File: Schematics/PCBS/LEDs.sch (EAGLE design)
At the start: 13 parts, among them IC1 ATMEGA328P-AU, Q1 TRANSISTOR-FET_DMN2004K, Q2 TRANSISTOR-FET_DMN2004K, Q3 TRANSISTOR-FET_DMN2004K, Q4 TRANSISTOR-FET_DMN2004K, Q5 TRANSISTOR-FET_DMN2004K, Q6 TRANSISTOR-FET_DMN2004K, Q7 TRANSISTOR-FET_DMN2004K, Q8 TRANSISTOR-FET_DMN2004K, Q9 TRANSISTOR-FET_DMN2004K

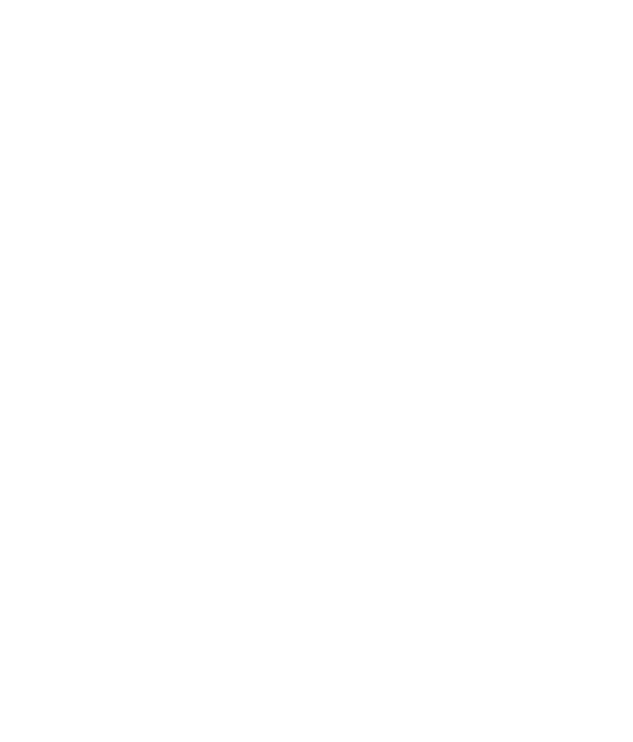
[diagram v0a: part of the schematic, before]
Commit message: added power rail and regulator
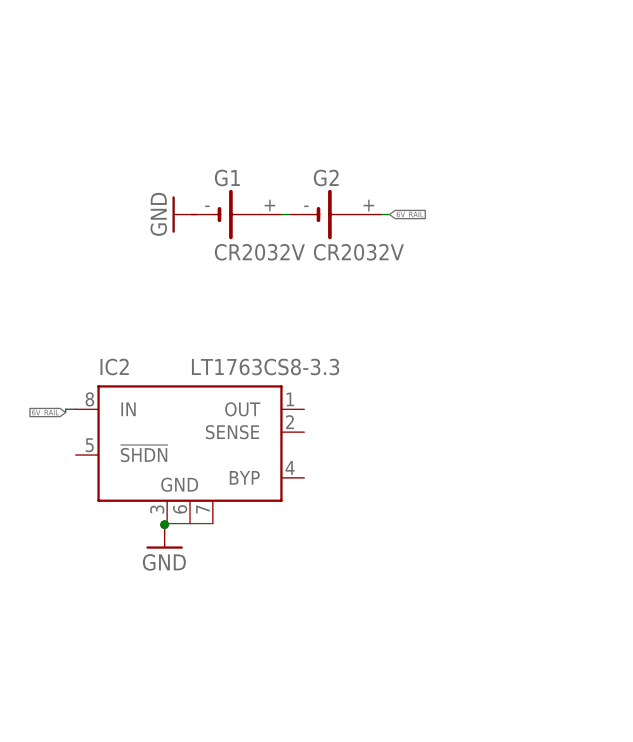
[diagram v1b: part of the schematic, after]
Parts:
- added G1, G2: CR2032V, battery:CR2032V
- added IC2: LT1763CS8-3.3, linear-technology:LT1763CS8-3.3
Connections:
- new net 6V_RAIL: G2.+, IC2.IN
- new net N$19: G1.+, G2.-
- net GND: now also IC2.GND@3
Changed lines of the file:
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@@
 <setting verticaltext="up"/>
 </settings>
-<grid distance="0.1" unitdist="inch" unit="inch" style="lines" multiple="1" display="no" altdistance="0.01" altunitdist="inch" altunit="inch"/>
+<grid distance="1" unitdist="mm" unit="mm" style="lines" multiple="1" display="yes" altdistance="0.000003125" altunitdist="mm" altunit="mm"/>
 <layers>
 <layer number="1" name="Top" color="4" fill="1" visible="no" active="no"/>
@@
 <part name="GND11" library="supply1" library_urn="urn:adsk.eagle:library:371" deviceset="GND" device=""/>
 <part name="GND12" library="supply1" library_urn="urn:adsk.eagle:library:371" deviceset="GND" device=""/>
+<part name="IC2" library="linear-technology" library_urn="urn:adsk.eagle:library:261" deviceset="LT1763CS8" device="" package3d_urn="urn:adsk.eagle:package:16057/2" technology="-3.3"/>
+<part name="GND14" library="supply1" library_urn="urn:adsk.eagle:library:371" deviceset="GND" device=""/>
+<part name="GND13" library="supply1" library_urn="urn:adsk.eagle:library:371" deviceset="GND" device=""/>
+<part name="G1" library="battery" library_urn="urn:adsk.eagle:library:109" deviceset="CR2032V" device="" package3d_urn="urn:adsk.eagle:package:4578/1"/>
+<part name="G2" library="battery" library_urn="urn:adsk.eagle:library:109" deviceset="CR2032V" device="" package3d_urn="urn:adsk.eagle:package:4578/1"/>
 </parts>
 <sheets>
@@
 <attribute name="VALUE" x="596.9" y="-33.02" size="1.778" layer="96" rot="R90"/>
 </instance>
+<instance part="IC2" gate="G$1" x="464.82" y="-43.18" smashed="yes">
+<attribute name="NAME" x="454.66" y="-36.83" size="1.778" layer="95"/>
+<attribute name="VALUE" x="464.82" y="-36.83" size="1.778" layer="96"/>
+</instance>
+<instance part="GND14" gate="1" x="462" y="-56" smashed="yes">
+<attribute name="VALUE" x="459.46" y="-58.54" size="1.778" layer="96"/>
+</instance>
+<instance part="GND13" gate="1" x="463" y="-19" smashed="yes" rot="R270">
+<attribute name="VALUE" x="460.46" y="-16.46" size="1.778" layer="96" rot="R270"/>
+</instance>
+<instance part="G1" gate="1" x="470" y="-19" smashed="yes">
+<attribute name="NAME" x="467.46" y="-15.825" size="1.778" layer="95"/>
+<attribute name="VALUE" x="467.46" y="-24.08" size="1.778" layer="96"/>
+</instance>
+<instance part="G2" gate="1" x="481" y="-19" smashed="yes">
+<attribute name="NAME" x="478.46" y="-15.825" size="1.778" layer="95"/>
+<attribute name="VALUE" x="478.46" y="-24.08" size="1.778" layer="96"/>
+</instance>
 </instances>
 <busses>
@@
 <pinref part="GND12" gate="1" pin="GND"/>
 </segment>
+<segment>
+<pinref part="IC2" gate="G$1" pin="GND@3"/>
+<wire x1="467.36" y1="-53.34" x2="462" y2="-53.34" width="0.1524" layer="91"/>
+<wire x1="462" y1="-53.34" x2="462" y2="-53.46" width="0.1524" layer="91"/>
+<pinref part="GND14" gate="1" pin="GND"/>
+<wire x1="462" y1="-53.46" x2="462" y2="-54" width="0.1524" layer="91"/>
+<junction x="462" y="-53.46"/>
+</segment>
 </net>
 <net name="N$10" class="0">
@@
 </segment>
 </net>
+<net name="6V_RAIL" class="0">
+<segment>
+<pinref part="IC2" gate="G$1" pin="IN"/>
+<wire x1="452.12" y1="-40.64" x2="451" y2="-40.64" width="0.1524" layer="91"/>
+<wire x1="451" y1="-40.64" x2="451" y2="-41" width="0.1524" layer="91"/>
+<label x="451" y="-41" size="0.6096" layer="95" rot="R180" xref="yes"/>
+</segment>
+<segment>
+<pinref part="G2" gate="1" pin="+"/>
+<wire x1="486.08" y1="-19" x2="487" y2="-19" width="0.1524" layer="91"/>
+<label x="487" y="-19" size="0.6096" layer="95" xref="yes"/>
+</segment>
+</net>
+<net name="N$19" class="0">
+<segment>
+<pinref part="G1" gate="1" pin="+"/>
+<pinref part="G2" gate="1" pin="-"/>
+<wire x1="475.08" y1="-19" x2="475.92" y2="-19" width="0.1524" layer="91"/>
+</segment>
+</net>

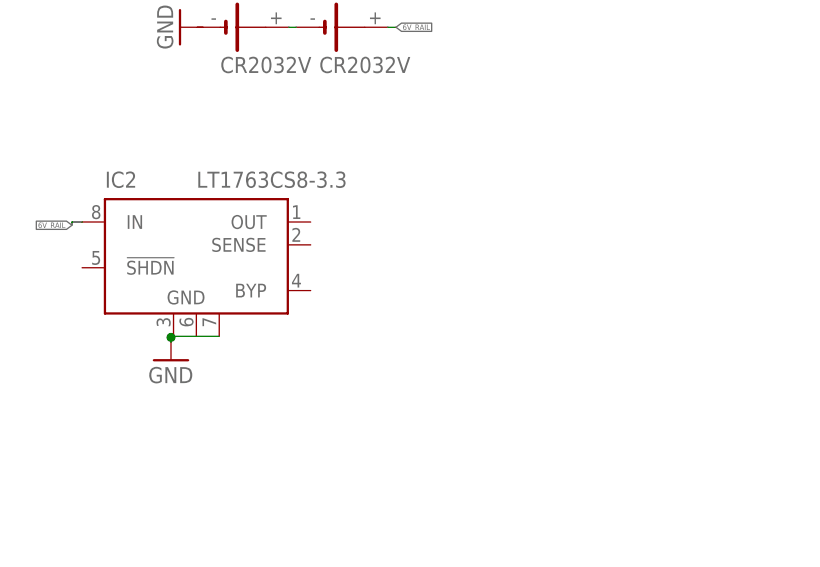
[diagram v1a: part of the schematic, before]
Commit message: LT1763CS8-5TRPBF.lbr and LT1763CS8-3.3_TRPBF.lbr2. Also updated Regulator in LED PCB to the correct variant
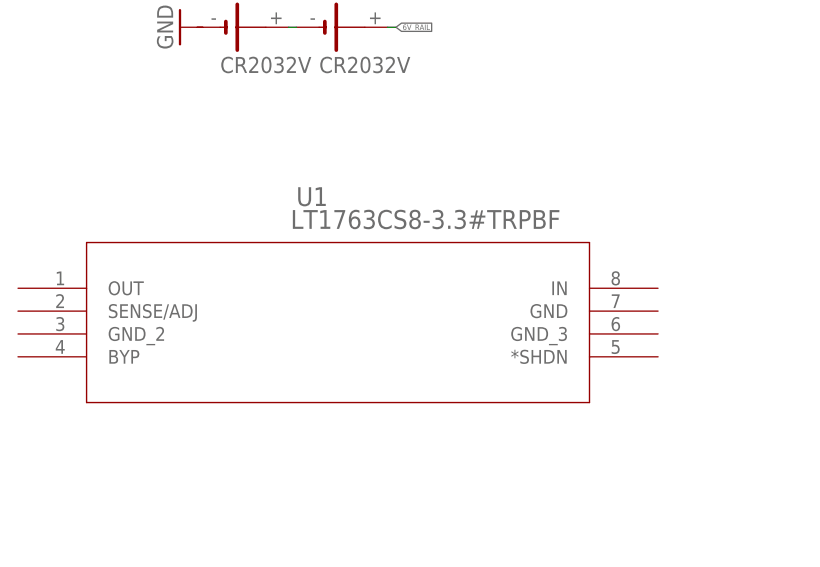
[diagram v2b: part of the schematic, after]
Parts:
- removed IC2: LT1763CS8-3.3, linear-technology:LT1763CS8-3.3
- added U1: LT1763CS8-3.3#TRPBF, LT1763CS8-3.3_TRPBF:LT1763CS8-3.3#TRPBF
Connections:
- net 6V_RAIL: no longer IC2.IN
- net GND: no longer IC2.GND@3
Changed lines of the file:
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@@
 <part name="GND11" library="supply1" library_urn="urn:adsk.eagle:library:371" deviceset="GND" device=""/>
 <part name="GND12" library="supply1" library_urn="urn:adsk.eagle:library:371" deviceset="GND" device=""/>
-<part name="IC2" library="linear-technology" library_urn="urn:adsk.eagle:library:261" deviceset="LT1763CS8" device="" package3d_urn="urn:adsk.eagle:package:16057/2" technology="-3.3"/>
-<part name="GND14" library="supply1" library_urn="urn:adsk.eagle:library:371" deviceset="GND" device=""/>
 <part name="GND13" library="supply1" library_urn="urn:adsk.eagle:library:371" deviceset="GND" device=""/>
 <part name="G1" library="battery" library_urn="urn:adsk.eagle:library:109" deviceset="CR2032V" device="" package3d_urn="urn:adsk.eagle:package:4578/1"/>
 <part name="G2" library="battery" library_urn="urn:adsk.eagle:library:109" deviceset="CR2032V" device="" package3d_urn="urn:adsk.eagle:package:4578/1"/>
+<part name="U1" library="LT1763CS8-3.3_TRPBF" deviceset="LT1763CS8-3.3#TRPBF" device=""/>
 </parts>
 <sheets>
@@
 <attribute name="VALUE" x="596.9" y="-33.02" size="1.778" layer="96" rot="R90"/>
 </instance>
-<instance part="IC2" gate="G$1" x="464.82" y="-43.18" smashed="yes">
-<attribute name="NAME" x="454.66" y="-36.83" size="1.778" layer="95"/>
-<attribute name="VALUE" x="464.82" y="-36.83" size="1.778" layer="96"/>
-</instance>
-<instance part="GND14" gate="1" x="462" y="-56" smashed="yes">
-<attribute name="VALUE" x="459.46" y="-58.54" size="1.778" layer="96"/>
-</instance>
 <instance part="GND13" gate="1" x="463" y="-19" smashed="yes" rot="R270">
 <attribute name="VALUE" x="460.46" y="-16.46" size="1.778" layer="96" rot="R270"/>
@@
 <attribute name="NAME" x="478.46" y="-15.825" size="1.778" layer="95"/>
 <attribute name="VALUE" x="478.46" y="-24.08" size="1.778" layer="96"/>
+</instance>
+<instance part="U1" gate="A" x="445" y="-48" smashed="yes">
+<attribute name="NAME" x="475.909" y="-38.85968125" size="2.087759375" layer="95" ratio="6" rot="SR0"/>
+<attribute name="VALUE" x="475.2876" y="-41.402459375" size="2.0888" layer="96" ratio="6" rot="SR0"/>
 </instance>
 </instances>
@@
 <pinref part="GND12" gate="1" pin="GND"/>
 </segment>
-<segment>
-<pinref part="IC2" gate="G$1" pin="GND@3"/>
-<wire x1="467.36" y1="-53.34" x2="462" y2="-53.34" width="0.1524" layer="91"/>
-<wire x1="462" y1="-53.34" x2="462" y2="-53.46" width="0.1524" layer="91"/>
-<pinref part="GND14" gate="1" pin="GND"/>
-<wire x1="462" y1="-53.46" x2="462" y2="-54" width="0.1524" layer="91"/>
-<junction x="462" y="-53.46"/>
-</segment>
 </net>
 <net name="N$10" class="0">
@@
 <net name="6V_RAIL" class="0">
 <segment>
-<pinref part="IC2" gate="G$1" pin="IN"/>
-<wire x1="452.12" y1="-40.64" x2="451" y2="-40.64" width="0.1524" layer="91"/>
-<wire x1="451" y1="-40.64" x2="451" y2="-41" width="0.1524" layer="91"/>
-<label x="451" y="-41" size="0.6096" layer="95" rot="R180" xref="yes"/>
-</segment>
-<segment>
 <pinref part="G2" gate="1" pin="+"/>

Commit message: update power Rail
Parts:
- added C1: 10uf, adafruit:CPOL-USE1.8-4
- D1, D2, D3: SPICEPREFIX (none) -> E
- G1, G2: SPICEPREFIX (none) -> J
- IC1, U1: SPICEPREFIX (none) -> X
- Q1, Q2, Q3, Q4, Q5, Q6, Q7, Q8, Q9: SPICEPREFIX (none) -> Q
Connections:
- new net 3.3_RAIL: C1.+, U1.OUT, U1.SENSE/ADJ
- new net 6_RAIL: U1.*SHDN
- new net N$20: U1.GND, U1.GND_3
- net 6V_RAIL: now also U1.IN
- net GND: now also C1.-, U1.GND_2
